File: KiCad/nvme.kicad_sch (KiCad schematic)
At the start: 40 parts, among them J10 Bus_M.2_Socket_M, J11 Bus_M.2_Socket_M, J12 Bus_M.2_Socket_M, J13 Bus_M.2_Socket_M, J14 Bus_M.2_Socket_M

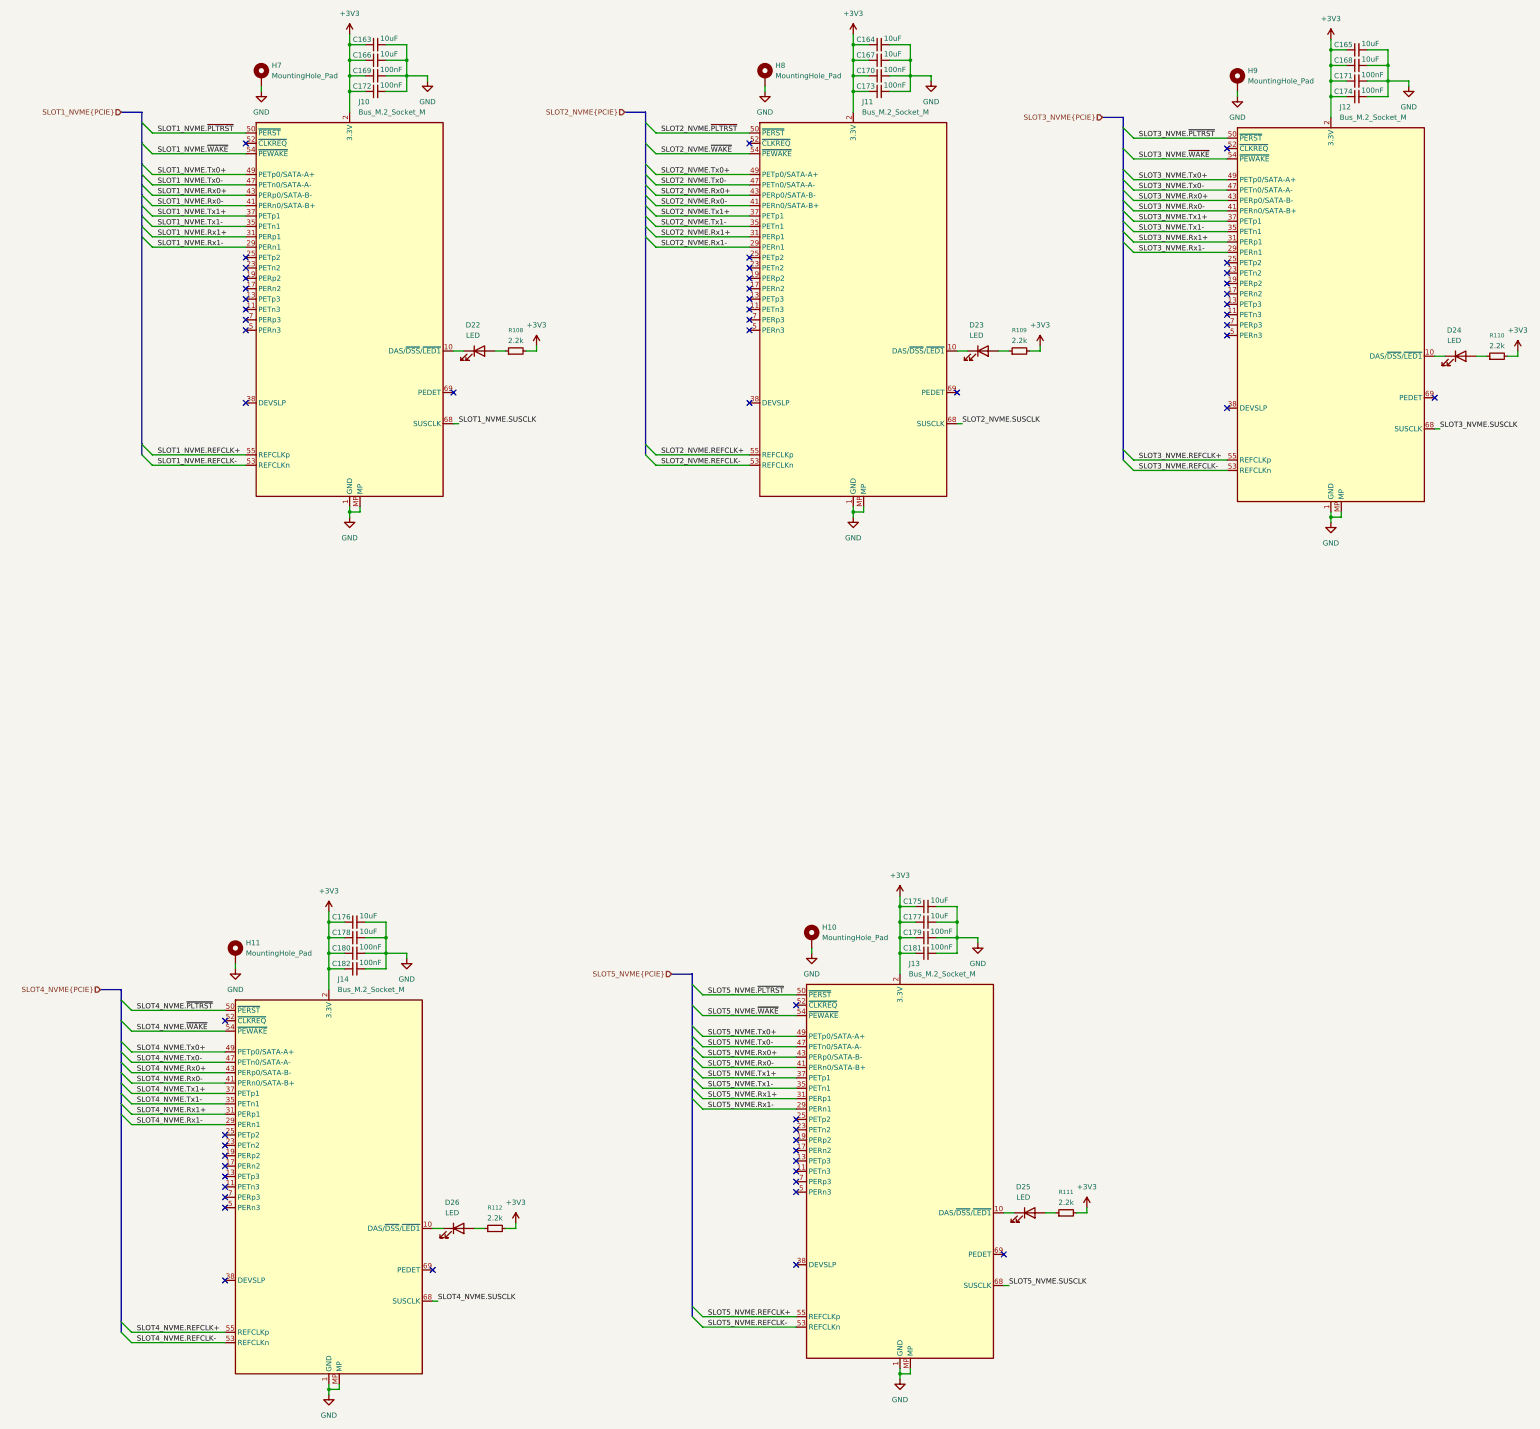
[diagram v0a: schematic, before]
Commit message: Re-annotate schematic
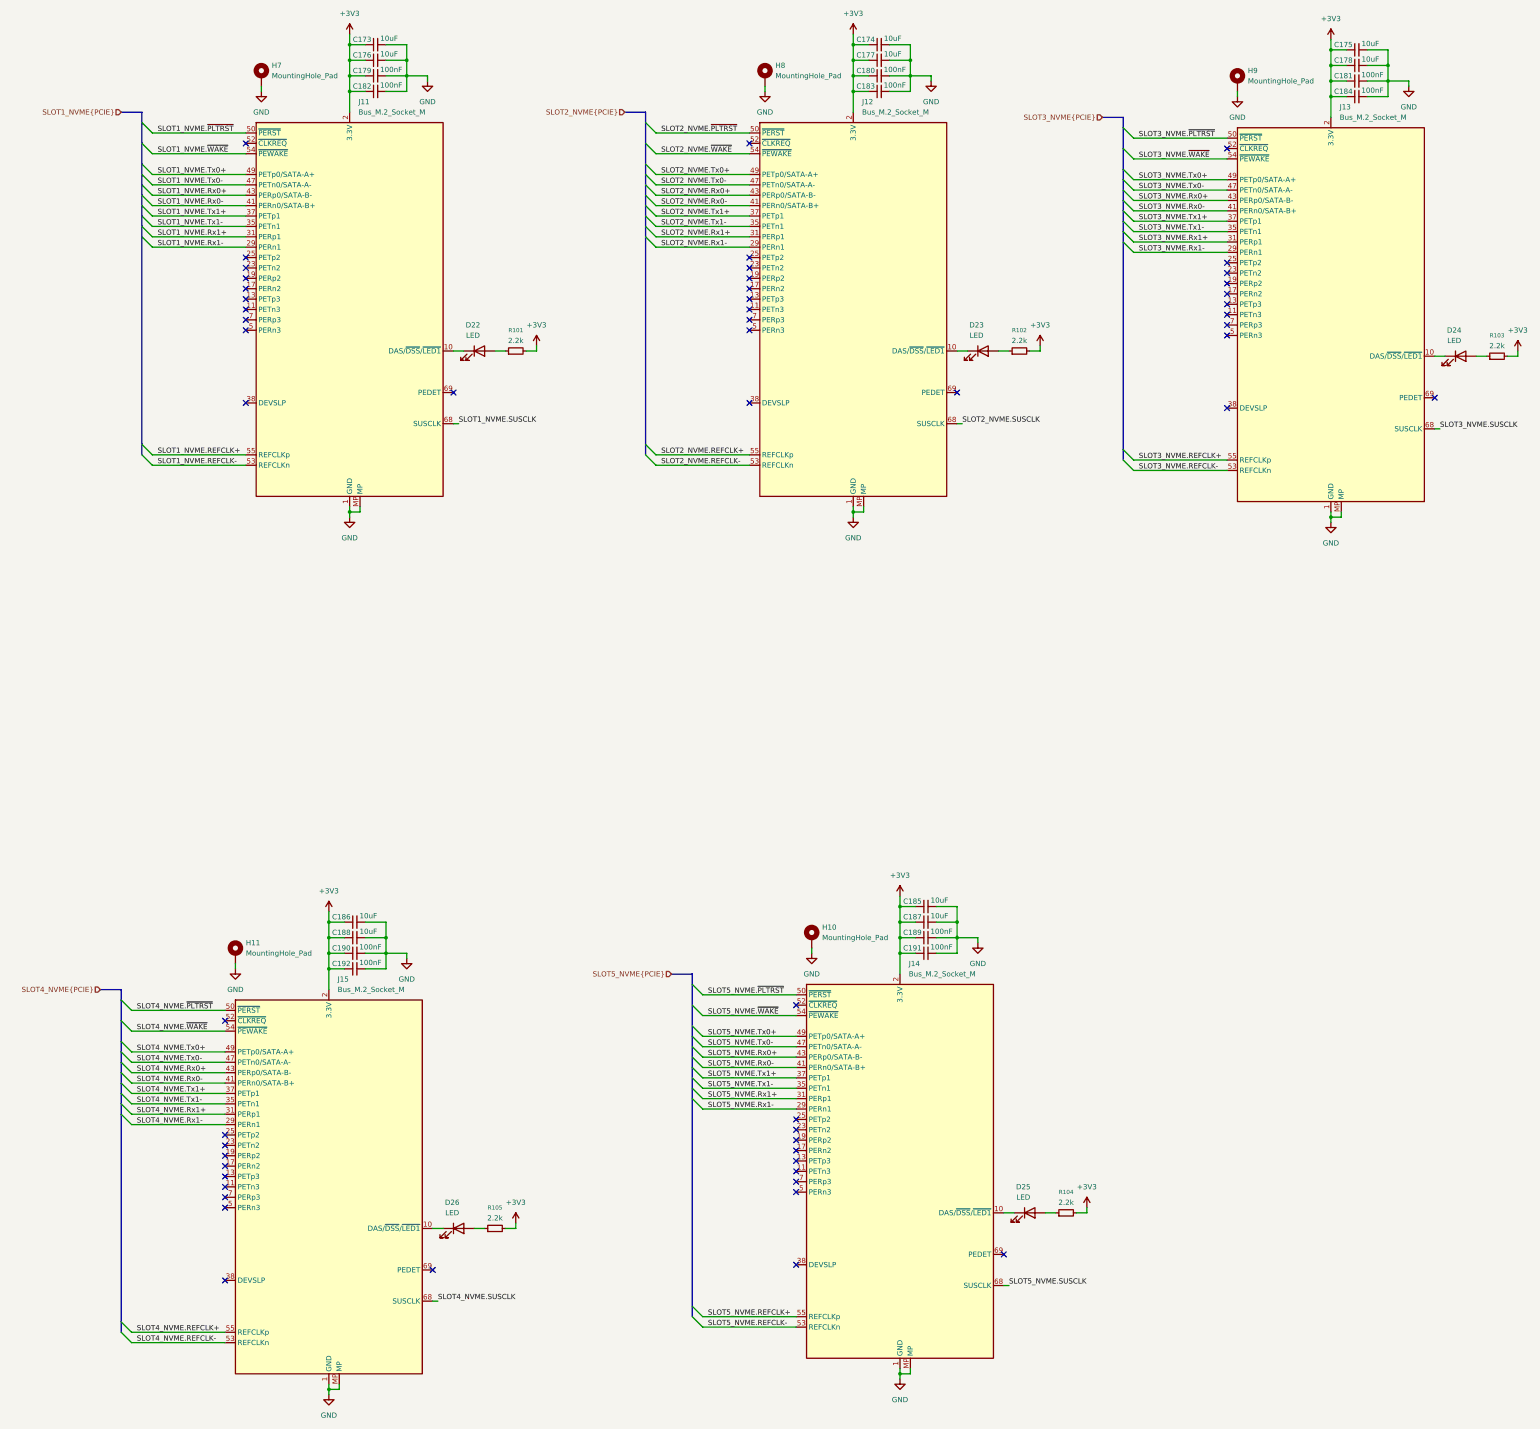
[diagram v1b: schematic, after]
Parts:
- renumbered C163 to C173, C164 to C174, C165 to C175, C166 to C176, C167 to C177, C168 to C178, C169 to C179, C170 to C180, C171 to C181, C172 to C182, C173 to C183, C174 to C184, C175 to C185, C176 to C186, C177 to C187, C178 to C188, C179 to C189, C180 to C190, C181 to C191, C182 to C192, J10 to J11, J11 to J12, J12 to J13, J13 to J14, J14 to J15, R108 to R101, R109 to R102, R110 to R103, R111 to R104, R112 to R105

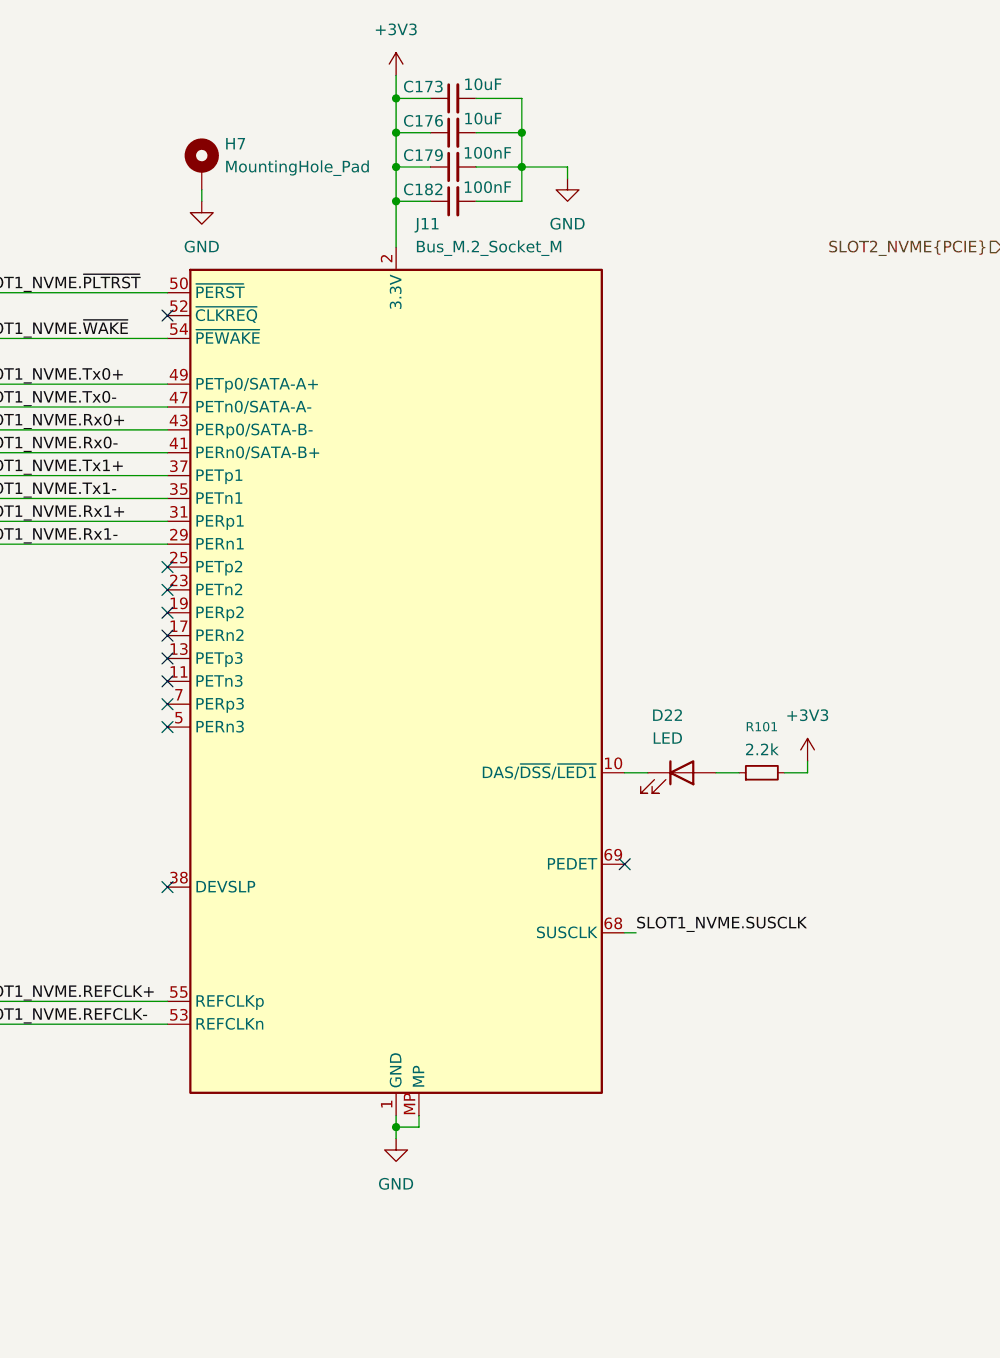
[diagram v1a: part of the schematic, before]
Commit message: Begin moving IO to module sheets
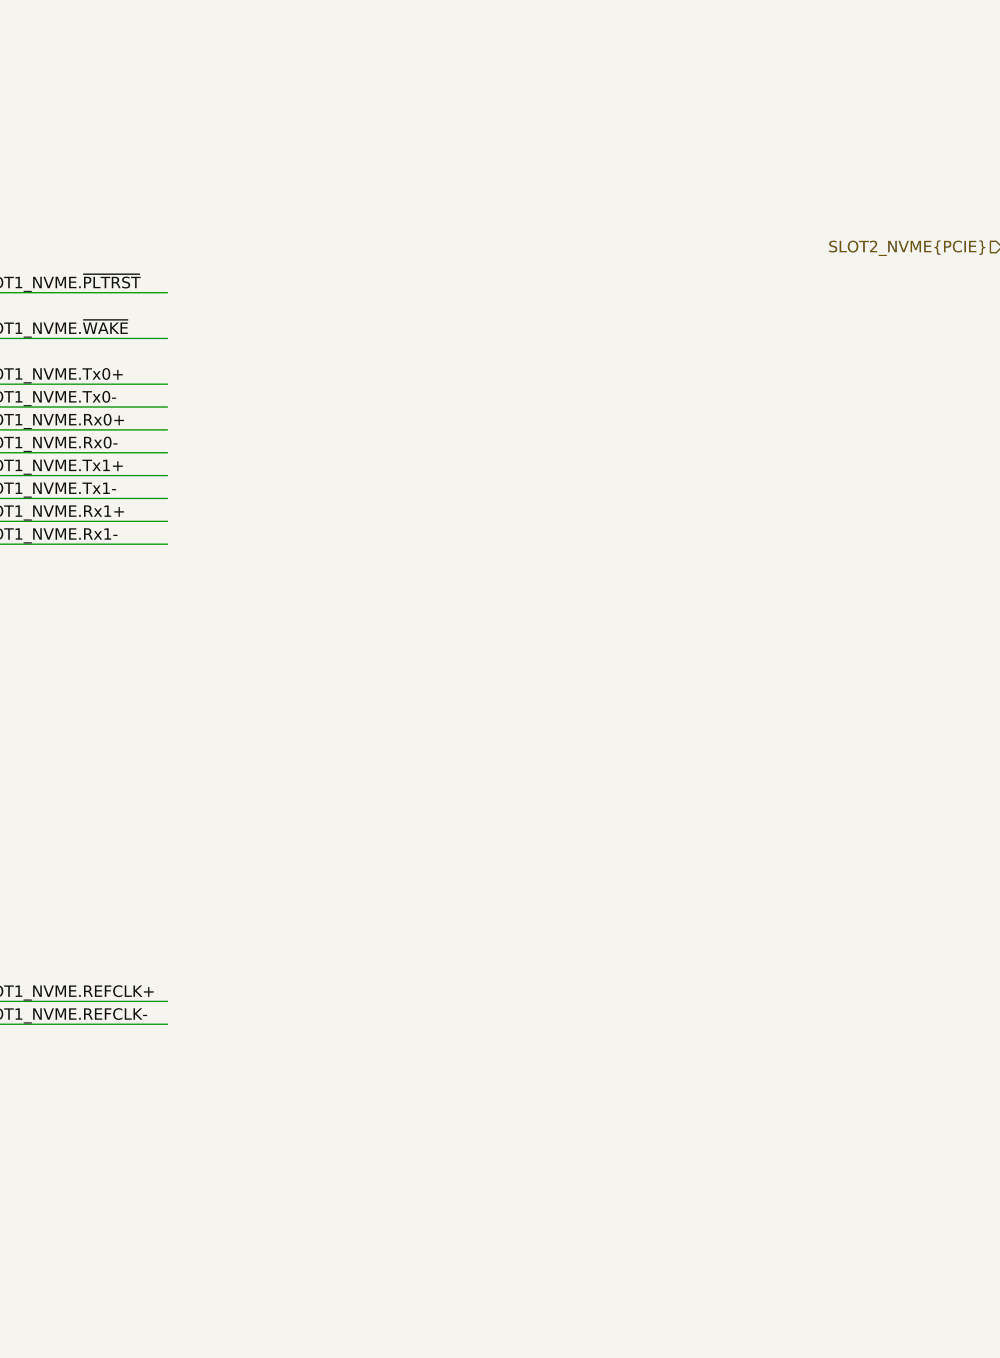
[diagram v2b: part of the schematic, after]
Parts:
- removed C173, C176: 10uF, Capacitor_SMD:C_0603_1608Metric, symbol Device:C_Small
- removed C179, C182: 100nF, Capacitor_SMD:C_0402_1005Metric, symbol Device:C_Small
- removed D22: LED, LED_SMD:LED_0603_1608Metric, symbol Device:LED
- removed H7: MountingHole_Pad, MountingHole:MountingHole_2.2mm_M2_Pad_Via, symbol Mechanical:MountingHole_Pad
- removed J11: Bus_M.2_Socket_M, EasyEDA2KiCAD:CONN-SMD_AS0BC21-S30BM-7H, symbol Connector:Bus_M.2_Socket_M
- removed R101: 2.2k, Resistor_SMD:R_0402_1005Metric, symbol Device:R_Small
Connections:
- no-connect marks 55 -> 44
